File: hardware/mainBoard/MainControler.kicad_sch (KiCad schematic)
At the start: 37 parts, among them J2 Conn_01x10_Pin, J20 1935161, J21 1935161, J23 1935161, J24 1935161, J25 1935161, J6 Conn_01x20_Socket, U13 TCMT1109, U14 TCMT1109, U4 ESP32-S3-DevKitC, U5 SX1509

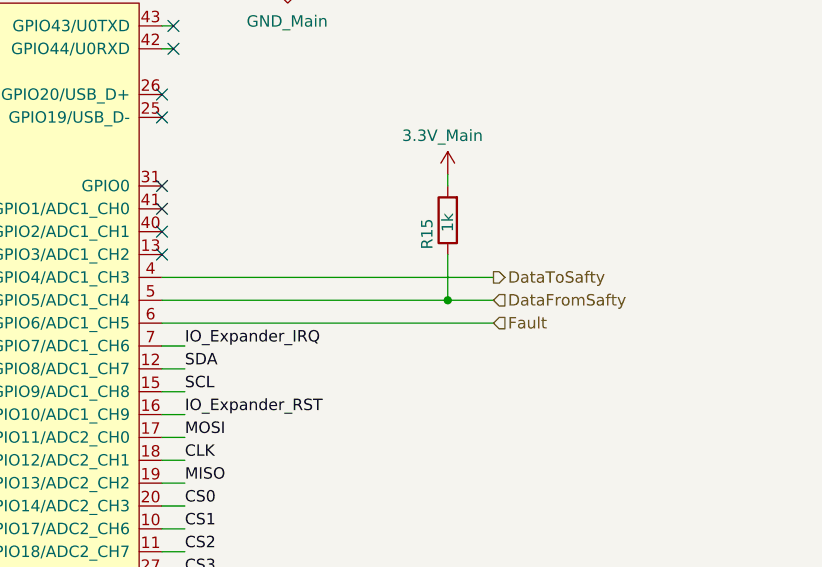
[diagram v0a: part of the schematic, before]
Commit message: Safety link: the isolated UART pin map, measured instead of traced
The ESP's safety-link TX/RX were swapped relative to the board, and had
been since the pin defaults were set. The link could not work in either
direction: the ESP transmitted into U3's collector and listened on U2's
LED drive. Correct map, now measured on the bench rather than derived
from the schematic:

  ESP GPIO5 = TX (DataToSafty, drives U2's LED through R12)
  ESP GPIO4 = RX (DataFromSafty, U3's collector, R15 pull-up)

Schematic and board
-------------------
Three faults, all fixed here and reworked on the physical board:

  - The top-level sheet crossed the two hierarchical pins: MainControler's
    DataToSafty (an output) was wired to SaftyProcessor's DataFromSafty
    (also an output), and the two inputs were wired to each other. That
    collapsed the two names into one net, which KiCad named after the
    main sheet, so the same wire appeared under both names depending on
    which sheet you read.
  - The MainControler sheet's labels were swapped relative to the safety
    sheet's. They now agree: U3's collector is DataFromSafty everywhere,
    R12's net is DataToSafty everywhere.
  - R15 (1k to 3.3V_Main) sat on the TX net, where a pull-up does nothing,
    while the RX collector had none. Moved onto GPIO4, mirroring R9's role
    on the safety side.

The measurement
---------------
Coordinated two-board GPIO test, each processor reached by a path that is
not the link under test (ESP over its USB-serial bridge and JTAG, Pico
over SWD). Every crossing inverts, as predicted:

  ESP GPIO5 high  -> Pico GP5 low    (U2's LED lit)
  ESP GPIO5 low   -> Pico GP5 high   (R9 pulls up)
  Pico GP4 high   -> ESP GPIO4 low   (U3's LED lit)
  Pico GP4 low    -> ESP GPIO4 high  (R15 pulls up)
  Pico GP5 driven -> no change at the ESP (its own receiver)
  ESP GPIO6 high  -> Pico GP10 low   (U1's LED lit)
  ESP in reset    -> Pico GP10 high  (R8 pulls up)

Corroborated at register level: ESP GPIO_IN_REG 0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
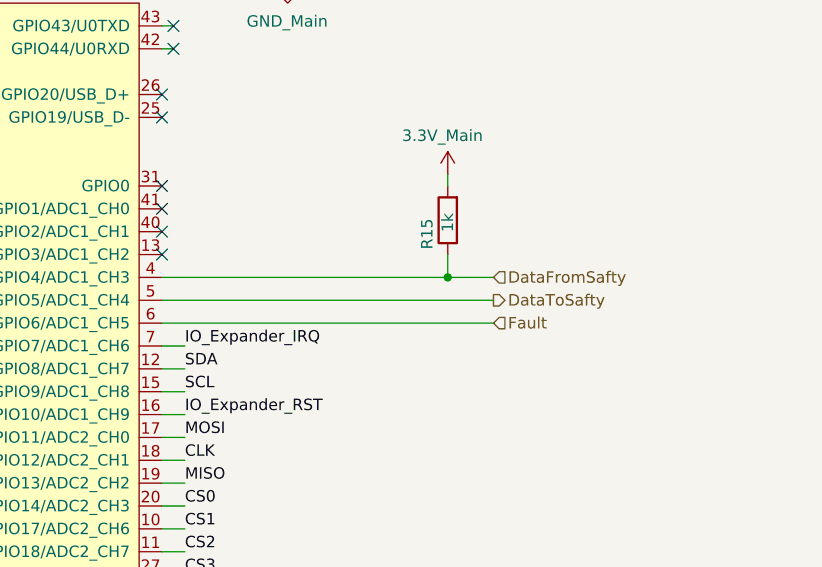
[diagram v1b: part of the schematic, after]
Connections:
- net DataFromSafty: now also U4.4 (GPIO4/ADC1_CH3); no longer U4.5 (GPIO5/ADC1_CH4)
- net DataToSafty: now also U4.5 (GPIO5/ADC1_CH4); no longer U4.4 (GPIO4/ADC1_CH3)
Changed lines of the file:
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@@
 	)
 	(junction
-		(at 265.43 208.28)
+		(at 250.19 86.36)
 		(diameter 0)
 		(color 0 0 0 0)
 	)
 	(junction
-		(at 223.52 236.22)
+		(at 265.43 208.28)
 		(diameter 0)
 		(color 0 0 0 0)
 	)
 	(junction
-		(at 234.95 254)
+		(at 223.52 236.22)
 		(diameter 0)
 		(color 0 0 0 0)
 	)
 	(junction
-		(at 234.95 208.28)
+		(at 234.95 254)
 		(diameter 0)
 		(color 0 0 0 0)
 	)
 	(junction
-		(at 250.19 88.9)
+		(at 234.95 208.28)
 		(diameter 0)
 		(color 0 0 0 0)
@@
 	(wire
 		(pts
-			(xy 218.44 86.36) (xy 255.27 86.36)
+			(xy 218.44 86.36) (xy 250.19 86.36)
 		)
 		(stroke
@@
 	(wire
 		(pts
+			(xy 250.19 86.36) (xy 255.27 86.36)
+		)
+		(stroke
+			(width 0)
+			(type default)
+		)
+	)
+	(wire
+		(pts
 			(xy 372.11 173.99) (xy 400.05 173.99)
 		)
@@
 	(wire
 		(pts
-			(xy 218.44 88.9) (xy 250.19 88.9)
+			(xy 218.44 88.9) (xy 255.27 88.9)
 		)
 		(stroke
@@
 	(wire
 		(pts
-			(xy 250.19 83.82) (xy 250.19 88.9)
-		)
-		(stroke
-			(width 0)
-			(type default)
-		)
-	)
-	(wire
-		(pts
 			(xy 262.89 228.6) (xy 271.78 228.6)
 		)
@@
 	(wire
 		(pts
-			(xy 405.13 101.6) (xy 407.67 101.6)
+			(xy 250.19 83.82) (xy 250.19 86.36)
 		)
 		(stroke
@@
 	(wire
 		(pts
-			(xy 372.11 176.53) (xy 402.59 176.53)
+			(xy 405.13 101.6) (xy 407.67 101.6)
 		)
 		(stroke
@@
 	(wire
 		(pts
-			(xy 107.95 36.83) (xy 100.33 36.83)
+			(xy 372.11 176.53) (xy 402.59 176.53)
 		)
 		(stroke
@@
 	(wire
 		(pts
-			(xy 381 212.09) (xy 381 213.36)
+			(xy 107.95 36.83) (xy 100.33 36.83)
 		)
 		(stroke
@@
 	(wire
 		(pts
-			(xy 90.17 55.88) (xy 92.71 55.88)
+			(xy 381 212.09) (xy 381 213.36)
 		)
 		(stroke
@@
 	(wire
 		(pts
-			(xy 387.35 101.6) (xy 387.35 102.87)
+			(xy 90.17 55.88) (xy 92.71 55.88)
 		)
 		(stroke
@@
 	(wire
 		(pts
-			(xy 106.68 156.21) (xy 111.76 156.21)
+			(xy 387.35 101.6) (xy 387.35 102.87)
 		)
 		(stroke
@@
 	(wire
 		(pts
-			(xy 250.19 88.9) (xy 255.27 88.9)
+			(xy 106.68 156.21) (xy 111.76 156.21)
 		)
 		(stroke
@@
 		)
 	)
-	(hierarchical_label "DataToSafty"
-		(shape output)
+	(hierarchical_label "DataFromSafty"
+		(shape input)
 		(at 255.27 86.36 0)
 		(effects
@@
 		)
 	)
-	(hierarchical_label "DataFromSafty"
-		(shape input)
+	(hierarchical_label "DataToSafty"
+		(shape output)
 		(at 255.27 88.9 0)
 		(effects

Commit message: Safety link: ADuM1201 replaces the optocouplers, and 9600 was never our limit
The TCMT1109 pair (U2/U3 with R7/R12/R15) that carried the ESP<->RP2040
UART is gone, replaced by one ADuM1201WT digital isolator, U6. Two
properties of that part drove every firmware change here:

  - It does not invert. Each optocoupler did, which is why both ends
    inverted their own TX to cancel it. With a non-inverting barrier
    those cancellations have nothing to cancel, so keeping either one
    parks the far end's RX in a permanent break. Measured with the
    isolator fitted and the old inversions still in place: sent 18,
    received 0, crc/framing errors 33 and climbing, Pico RX pad low on
    2954 of 3000 samples. Both inversions removed:
    uart_set_line_inverse(TXD_INV) from safety_link.c and
    gpio_set_outover(GPIO_OVERRIDE_INVERT) from uart_owner.c.

  - It is fast. The 9600 ceiling was a property of the optocouplers, not
    of either firmware, and every doc that said otherwise was wrong.
    A descending sweep of the standard rates, 60s continuous per rate,
    judged on crc/framing + length-mismatch + crc-mismatch + resync
    deltas: 921600, 460800 and 230400 all clean, zero new errors, status
    replies answering every 500ms poll. Committed value is 230400 -- one
    standard step below the fastest pass is 460800, and 230400 is the
    slower of that and the requested 230400. Two full standard steps of
    margin below a rate that soaks clean.

Also found, while reading the code this change touches: the bootloader's
recovery mode never applied the TX inversion the application did, and its
comment claimed the two matched. Under the optocouplers recovery mode's
Pico->ESP polarity was therefore inverted relative to the application.
Both are non-inverting now, so recovery mode is correct for the first
time -- documented in bootloader/main.c rather than silently fixed.

Baud is hardcoded in three places that must agree, now called out in each:
KilnFW's KILNCTL_SAFET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
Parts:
- removed R15: 1k, Resistor_SMD:R_0402_1005Metric, symbol Device:R
